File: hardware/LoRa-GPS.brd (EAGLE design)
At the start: 50.8 x 17.8 mm, 30 parts, among them J1 10118193-0001LF, Q1 IRLML6402, U1 MCP1703-3302E/CB, Y1 CRYSTAL.ABS07

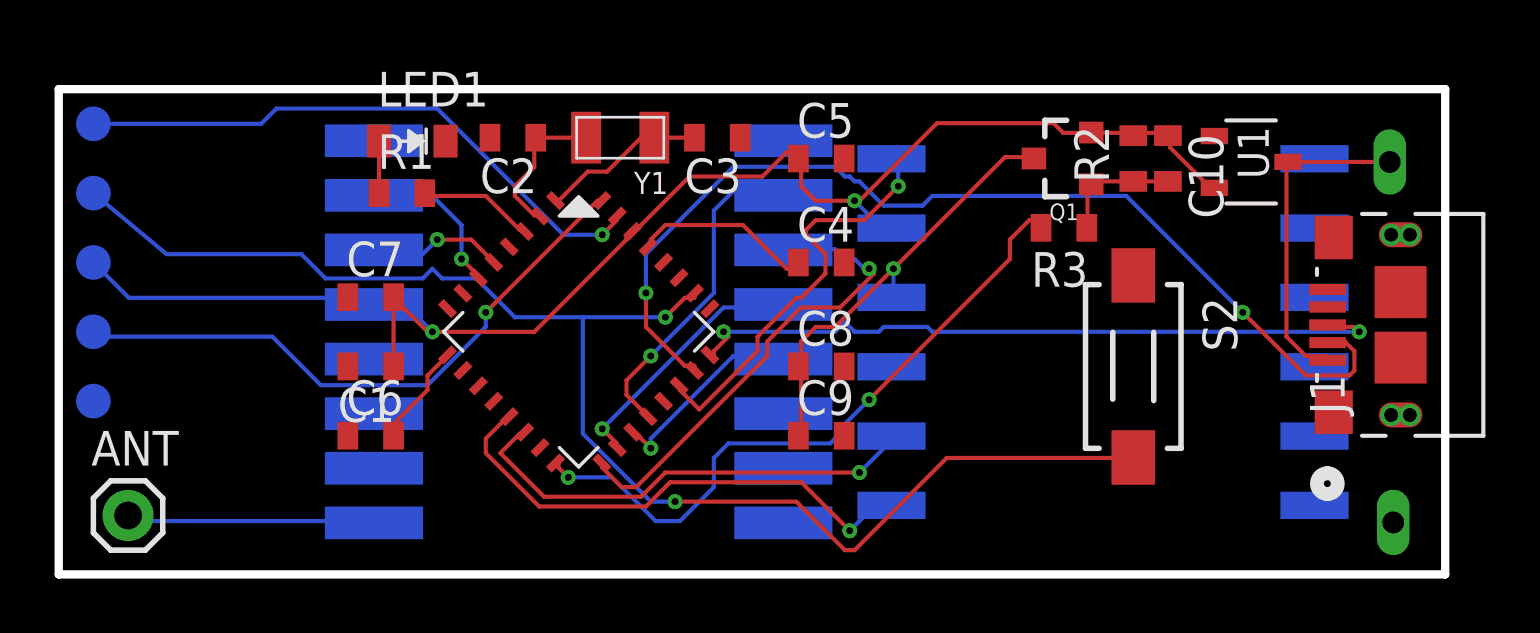
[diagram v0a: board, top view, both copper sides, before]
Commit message: manual route
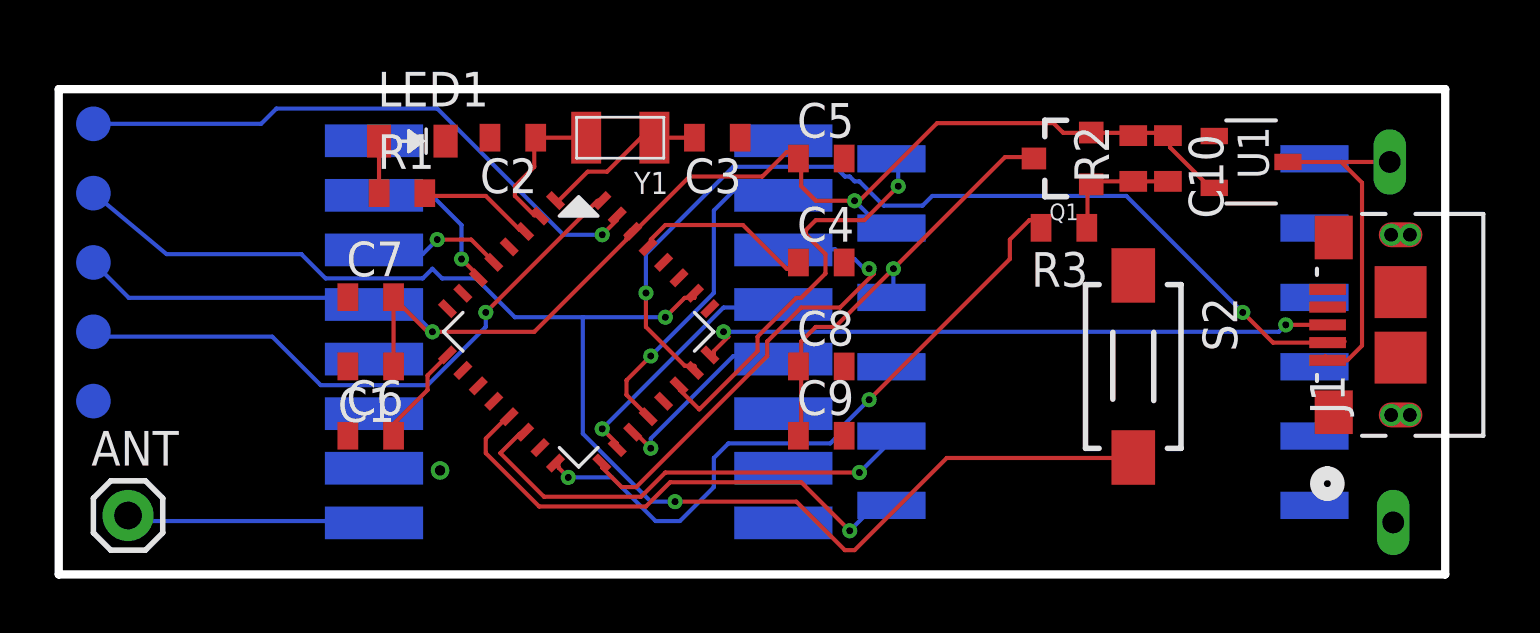
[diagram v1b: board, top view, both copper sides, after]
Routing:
- net D-: track 37.9 -> 35.1 mm
- net D+: track 26.3 -> 23.7 mm
- net GND: vias 0 -> 1
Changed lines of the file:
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@@
 <wire x1="22.225" y1="11.557" x2="22.16126875" y2="11.435584375" width="0.1524" layer="1"/>
 <wire x1="22.225" y1="11.557" x2="22.253853125" y2="11.528146875" width="0.1524" layer="1"/>
-<wire x1="10.5918" y1="5.08" x2="11.55" y2="3.89" width="0" layer="19" extent="1-16"/>
+<via x="13.97" y="3.81" extent="1-16" drill="0.381"/>
 </signal>
 <signal name="VCC">
@@
 <contactref element="JP1" pad="P$1"/>
 <contactref element="J1" pad="1"/>
-<wire x1="48.768" y1="15.113" x2="45.038" y2="15.113" width="0.1524" layer="1"/>
-<wire x1="45.6946" y1="8.001" x2="46.4058" y2="8.001" width="0.1524" layer="1"/>
-<wire x1="44.9834" y1="8.7122" x2="45.6946" y2="8.001" width="0.1524" layer="1"/>
-<wire x1="44.9834" y1="15.113" x2="44.9834" y2="8.7122" width="0.1524" layer="1"/>
+<wire x1="48.768" y1="15.113" x2="46.99" y2="15.113" width="0.1524" layer="1"/>
+<wire x1="46.99" y1="15.113" x2="45.038" y2="15.113" width="0.1524" layer="1"/>
 <wire x1="46.4058" y1="8.001" x2="46.4903" y2="7.844" width="0.1524" layer="1"/>
 <wire x1="44.9834" y1="15.113" x2="45.038" y2="15.113" width="0.1524" layer="1"/>
+<wire x1="46.99" y1="15.113" x2="47.752" y2="14.351" width="0.1524" layer="1"/>
+<wire x1="47.752" y1="14.351" x2="47.752" y2="8.382" width="0.1524" layer="1"/>
+<wire x1="47.752" y1="8.382" x2="47.214" y2="7.844" width="0.1524" layer="1"/>
+<wire x1="47.214" y1="7.844" x2="46.4903" y2="7.844" width="0.1524" layer="1"/>
 </signal>
 <signal name="D-">
@@
 <wire x1="39.116" y1="13.8684" x2="32.004" y2="13.8684" width="0.1524" layer="16"/>
 <wire x1="43.3832" y1="9.6012" x2="39.116" y2="13.8684" width="0.1524" layer="16"/>
-<wire x1="45.6946" y1="7.2898" x2="43.3832" y2="9.6012" width="0.1524" layer="1"/>
-<wire x1="47.2948" y1="7.2898" x2="45.6946" y2="7.2898" width="0.1524" layer="1"/>
-<wire x1="47.4726" y1="7.4676" x2="47.2948" y2="7.2898" width="0.1524" layer="1"/>
-<wire x1="47.4726" y1="8.1788" x2="47.4726" y2="7.4676" width="0.1524" layer="1"/>
-<wire x1="47.117" y1="8.5344" x2="47.4726" y2="8.1788" width="0.1524" layer="1"/>
 <wire x1="46.5836" y1="8.5344" x2="47.117" y2="8.5344" width="0.1524" layer="1"/>
 <wire x1="23.2918" y1="7.6454" x2="23.292640625" y2="7.475784375" width="0.1524" layer="1"/>
@@
 <via x="21.5138" y="10.3124" extent="1-16" drill="0.254"/>
 <via x="43.3832" y="9.6012" extent="1-16" drill="0.254"/>
+<wire x1="43.3832" y1="9.6012" x2="44.4904" y2="8.494" width="0.1524" layer="1"/>
+<wire x1="44.4904" y1="8.494" x2="46.4903" y2="8.494" width="0.1524" layer="1"/>
 </signal>
 <signal name="D+">
@@
 <wire x1="24.5364" y1="8.7122" x2="24.003" y2="8.1788" width="0.1524" layer="1"/>
 <wire x1="24.3586" y1="8.89" x2="24.5364" y2="8.7122" width="0.1524" layer="1"/>
-<wire x1="28.448" y1="8.89" x2="24.3586" y2="8.89" width="0.1524" layer="16"/>
-<wire x1="28.8036" y1="9.2456" x2="28.448" y2="8.89" width="0.1524" layer="16"/>
-<wire x1="29.1592" y1="8.89" x2="28.8036" y2="9.2456" width="0.1524" layer="16"/>
-<wire x1="30.0482" y1="8.89" x2="29.1592" y2="8.89" width="0.1524" layer="16"/>
-<wire x1="30.226" y1="9.0678" x2="30.0482" y2="8.89" width="0.1524" layer="16"/>
-<wire x1="31.8262" y1="9.0678" x2="30.226" y2="9.0678" width="0.1524" layer="16"/>
-<wire x1="32.004" y1="8.89" x2="31.8262" y2="9.0678" width="0.1524" layer="16"/>
-<wire x1="47.6504" y1="8.89" x2="32.004" y2="8.89" width="0.1524" layer="16"/>
-<wire x1="47.4726" y1="9.0678" x2="47.6504" y2="8.89" width="0.1524" layer="1"/>
-<wire x1="46.5836" y1="9.0678" x2="47.4726" y2="9.0678" width="0.1524" layer="1"/>
 <wire x1="24.003" y1="8.001" x2="23.858325" y2="8.04146875" width="0.1524" layer="1"/>
 <wire x1="46.5836" y1="9.0678" x2="46.4903" y2="9.144" width="0.1524" layer="1"/>
 <via x="24.3586" y="8.89" extent="1-16" drill="0.254"/>
-<via x="47.6504" y="8.89" extent="1-16" drill="0.254"/>
+<wire x1="46.4903" y1="9.144" x2="44.958" y2="9.144" width="0.1524" layer="1"/>
+<via x="44.958" y="9.144" extent="1-16" drill="0.254"/>
+<wire x1="44.958" y1="9.144" x2="44.704" y2="8.89" width="0.1524" layer="16"/>
+<wire x1="44.704" y1="8.89" x2="24.3586" y2="8.89" width="0.1524" layer="16"/>
 </signal>
 <signal name="N$1">

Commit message: sma
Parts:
- removed J1: 10118193-0001LF, usb:CONN_10118193-0001LF_AMP
- added J2: CON-SMA-EDGE-S, CON-SMA-EDGE-S:RFSOLUTIONS_CON-SMA-EDGE-S
- added J3: USB3085-XX-X_REVD, USB3085-XX-X_REVD:GCT_USB3085-XX-X_REVD
- ANT: value M01 -> (none); device nootropicdesign:1X01 -> wirepad:1,6/0,8
- moved ANT 5.09 mm to (7.62, 1.91)
- moved TP1 3.30 mm to (1.27, 9.65)
- moved TP5 2.54 mm to (1.27, 11.4)
- moved TP2 1.78 mm to (1.27, 13.2)
- moved JP1 0.90 mm to (48.9, 16.0)
- moved TP3 0.89 mm to (1.27, 14.9)
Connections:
- new net SHIELD: J3.6, J3.7, J3.8, J3.9
- net ANT: now also J2.1
- net D+: now also J3.3; no longer J1.3
- net D-: now also J3.2; no longer J1.2
- net GND: now also J2.G1, J2.G2, J2.G3, J2.G4, J3.5; no longer J1.5
- net VIN: now also J3.1; no longer J1.1
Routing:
- net SHIELD: track 0.00 -> 8.72 mm
- net VIN: track 12.5 -> 15.4 mm
- net SWDIO: track 22.9 -> 24.1 mm
- net ANT: track 9.10 -> 10.1 mm
- net VCC: track 54.9 -> 55.6 mm

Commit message: DRC pass
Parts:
- removed S2: DTSM-3, switch-tact:DTSM-3
- added S1: SKTHACE010, SamacSys_Parts:SKTHACE010
- moved Q1 1.27 mm to (35.6, 15.2)
- moved R2 1.27 mm to (38.1, 15.2)
- moved R3 1.27 mm to (35.6, 12.7)
- moved C10 0.51 mm to (40.1, 15.2)
- moved U1 0.38 mm to (43.3, 15.1)
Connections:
- net GND: now also S1.2, S1.4; no longer S2.1
- net RESET: now also S1.1, S1.3; no longer S2.2
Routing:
- net N$7: track 16.0 -> 15.0 mm
- net GPSPOWER: track 24.6 -> 23.6 mm
- net RESET: track 52.5 -> 53.4 mm
- net N$8: track 4.57 -> 5.42 mm
- net VIN: track 15.4 -> 16.1 mm

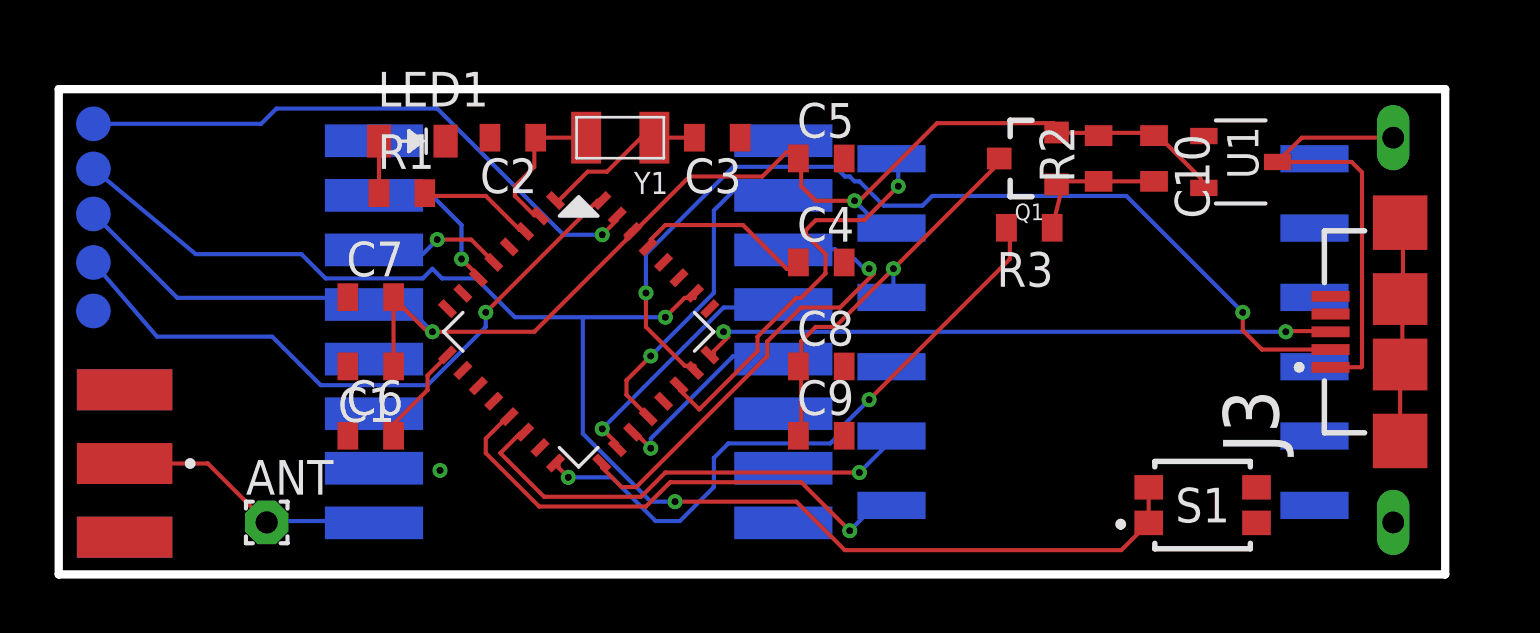
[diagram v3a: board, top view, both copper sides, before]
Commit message: bat mon. DRC keepout issue
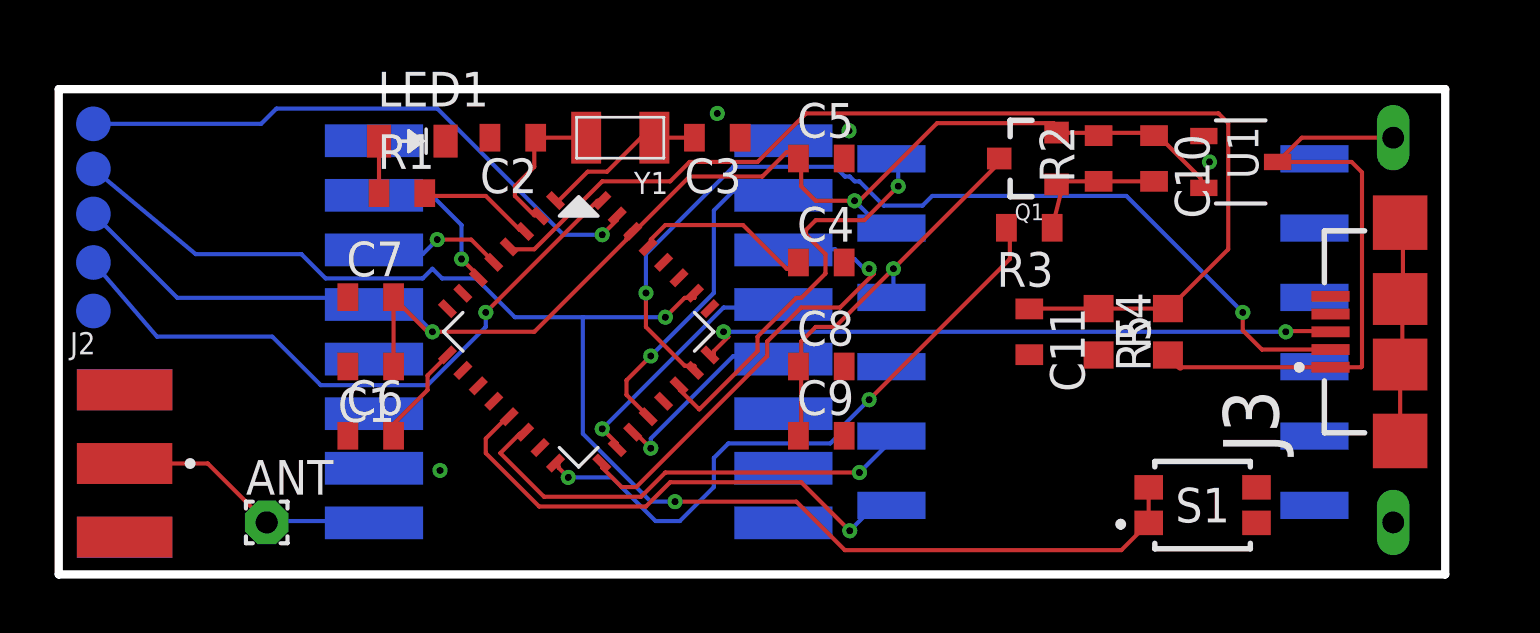
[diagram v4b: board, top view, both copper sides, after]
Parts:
- added C11: 100nF, nootropicdesign:C0603-THINCREAM
- added R4, R5: 1M, rcl:R0603
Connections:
- new net A4: C11.1, R4.2, R5.1, SAMD21.4
- net GND: now also C11.2, R5.2
- net VIN: now also R4.1
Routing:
- net A4: track 0.00 -> 41.4 mm
- net VIN: track 16.1 -> 22.3 mm
- net GND: vias 1 -> 4
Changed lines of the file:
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@@
 <drawing>
 <settings>
-<setting alwaysvectorfont="no"/>
+<setting alwaysvectorfont="yes"/>
 <setting keepoldvectorfont="yes"/>
 <setting verticaltext="up"/>
@@
 <attribute name="MF" value="RF Solutions" x="2.413" y="4.064" size="1.778" layer="27" font="vector" ratio="15" display="off"/>
 <attribute name="MP" value="CON-SMA-EDGE-S" x="2.413" y="4.064" size="1.778" layer="27" font="vector" ratio="15" display="off"/>
+<attribute name="NAME" x="0.413" y="8.064" size="0.8128" layer="26"/>
 <attribute name="NAME" x="0.413" y="8.064" size="0.8128" layer="25"/>
-<attribute name="NAME" x="0.413" y="8.064" size="0.8128" layer="26"/>
 <attribute name="PACKAGE" value="None" x="2.413" y="4.064" size="1.778" layer="27" font="vector" ratio="15" display="off"/>
 <attribute name="PRICE" value="None" x="2.413" y="4.064" size="1.778" layer="27" font="vector" ratio="15" display="off"/>
@@
 <attribute name="NAME" x="41.91" y="2.54" size="1.27" layer="25" align="center"/>
 <attribute name="VALUE" x="41.91" y="2.54" size="1.27" layer="27" align="center"/>
+</element>
+<element name="R4" library="rcl" library_urn="urn:adsk.eagle:library:334" package="R0603" package3d_urn="urn:adsk.eagle:package:23555/3" value="1M" x="40.64" y="8.89" smashed="yes" rot="R90">
+<attribute name="NAME" x="40.005" y="8.255" size="1.27" layer="25" rot="R90"/>
+<attribute name="POPULARITY" value="77" x="40.64" y="8.89" size="1.778" layer="27" font="vector" ratio="15" rot="R90" display="off"/>
+<attribute name="SPICEPREFIX" value="R" x="40.64" y="8.89" size="1.778" layer="27" font="vector" ratio="15" rot="R90" display="off"/>
+<attribute name="VALUE" x="42.545" y="8.255" size="1.27" layer="27" rot="R90"/>
+</element>
+<element name="R5" library="rcl" library_urn="urn:adsk.eagle:library:334" package="R0603" package3d_urn="urn:adsk.eagle:package:23555/3" value="1M" x="38.1" y="8.89" smashed="yes" rot="R270">
+<attribute name="NAME" x="38.735" y="9.525" size="1.27" layer="25" rot="R270"/>
+<attribute name="POPULARITY" value="77" x="38.1" y="8.89" size="1.778" layer="27" font="vector" ratio="15" rot="R270" display="off"/>
+<attribute name="SPICEPREFIX" value="R" x="38.1" y="8.89" size="1.778" layer="27" font="vector" ratio="15" rot="R270" display="off"/>
+<attribute name="VALUE" x="36.195" y="9.525" size="1.27" layer="27" rot="R270"/>
+</element>
+<element name="C11" library="nootropicdesign" package="C0603-THINCREAM" value="100nF" x="35.56" y="8.89" smashed="yes" rot="R270">
+<attribute name="MF" value="AVX" x="35.56" y="8.89" size="1.778" layer="27" font="vector" ratio="15" rot="R270" display="off"/>
+<attribute name="MPN" value="02016D104KAT2A" x="35.56" y="8.89" size="1.778" layer="27" font="vector" ratio="15" rot="R270" display="off"/>
+<attribute name="NAME" x="36.322" y="9.779" size="1.27" layer="25" rot="R270"/>
+<attribute name="OC_FARNELL" value="1657913" x="35.56" y="8.89" size="1.778" layer="27" font="vector" ratio="15" rot="R270" display="off"/>
+<attribute name="VALUE" x="33.528" y="9.779" size="1.27" layer="27" rot="R270"/>
 </element>
 </elements>
@@
 <contactref element="S1" pad="2"/>
 <contactref element="S1" pad="4"/>
+<contactref element="R5" pad="2"/>
+<contactref element="C11" pad="2"/>
+<via x="28.956" y="16.256" extent="1-16" drill="0.254"/>
+<via x="42.164" y="15.113" extent="1-16" drill="0.254"/>
+<via x="24.13" y="16.891" extent="1-16" drill="0.254"/>
 </signal>
 <signal name="VCC">
@@
 <wire x1="47.752" y1="7.62" x2="47.722" y2="7.59" width="0.1524" layer="1"/>
 <wire x1="47.722" y1="7.59" x2="46.599" y2="7.59" width="0.1524" layer="1"/>
+<contactref element="R4" pad="1"/>
+<wire x1="40.64" y1="8.04" x2="41.09" y2="7.59" width="0.254" layer="1"/>
+<wire x1="41.09" y1="7.59" x2="46.599" y2="7.59" width="0.1524" layer="1"/>
 </signal>
 <signal name="D-">
@@
 <wire x1="49.149" y1="7.69" x2="49.149" y2="4.89" width="0.1524" layer="1"/>
 </signal>
+<signal name="A4">
+<contactref element="SAMD21" pad="4"/>
+<contactref element="R4" pad="2"/>
+<contactref element="R5" pad="1"/>
+<contactref element="C11" pad="1"/>
+<wire x1="40.64" y1="9.74" x2="38.1" y2="9.74" width="0.1524" layer="1"/>
+<wire x1="38.1" y1="9.74" x2="35.5718" y2="9.74" width="0.1524" layer="1"/>
+<wire x1="35.5718" y1="9.74" x2="35.56" y2="9.7282" width="0.254" layer="1"/>
+<wire x1="17.4244" y1="11.9126" x2="16.5354" y2="11.9126" width="0.1524" layer="1"/>
+<wire x1="19.9136" y1="14.4018" x2="17.4244" y2="11.9126" width="0.1524" layer="1"/>
+<wire x1="22.4028" y1="14.4018" x2="19.9136" y2="14.4018" width="0.1524" layer="1"/>
+<wire x1="23.114" y1="15.113" x2="22.4028" y2="14.4018" width="0.1524" layer="1"/>
+<wire x1="25.6032" y1="15.113" x2="23.114" y2="15.113" width="0.1524" layer="1"/>
+<wire x1="27.3812" y1="16.891" x2="25.6032" y2="15.113" width="0.1524" layer="1"/>
+<wire x1="42.4942" y1="16.891" x2="27.3812" y2="16.891" width="0.1524" layer="1"/>
+<wire x1="42.8498" y1="16.5354" x2="42.4942" y2="16.891" width="0.1524" layer="1"/>
+<wire x1="42.8498" y1="11.9126" x2="42.8498" y2="16.5354" width="0.1524" layer="1"/>
+<wire x1="40.7162" y1="9.779" x2="42.8498" y2="11.9126" width="0.1524" layer="1"/>
+<wire x1="16.5354" y1="11.9126" x2="16.5044125" y2="12.00126875" width="0.1524" layer="1"/>
+<wire x1="40.7162" y1="9.779" x2="40.64" y2="9.74" width="0.1524" layer="1"/>
+</signal>
 </signals>
